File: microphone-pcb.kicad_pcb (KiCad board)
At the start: 4 copper layers, 10.7 x 11 mm, 9 parts, among them J1 JST_SUR_1x5_BM05B-SURS-TB-LF-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

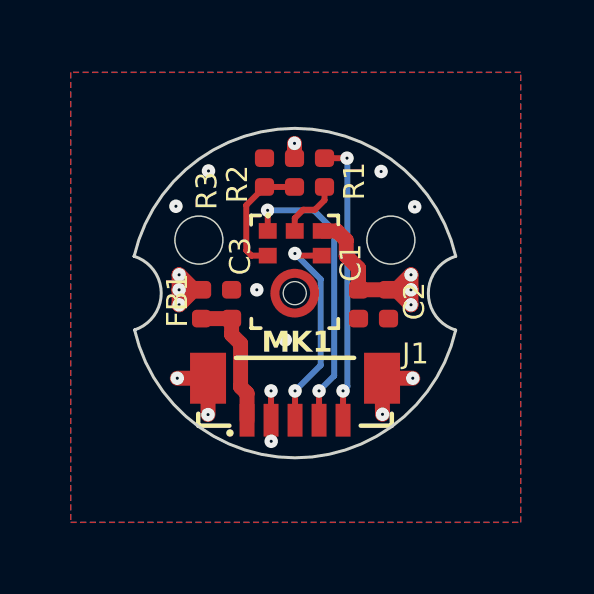
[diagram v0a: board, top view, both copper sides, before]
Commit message: [#71986]  Continue placement
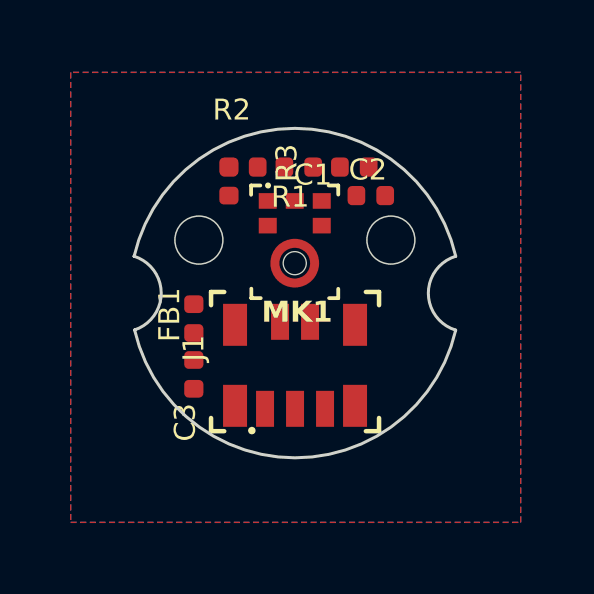
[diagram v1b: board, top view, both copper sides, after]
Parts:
- J1: value JST_SUR_1x5_BM05B-SURS-TB-LF-SN -> Conn_FFC_Molex_5019510550; footprint antmicro-footprints:Conn_JST_SUR_1x5_BM05B-SURS-TF-LF-SN -> antmicro-footprints:Conn_FFC_Molex_5019510550
- moved C1 4.57 mm to (242.0, 142.7), turned to 180 degrees
- moved C2 3.67 mm to (242.5, 143.7), turned to 0 degrees
- moved C3 2.66 mm to (236.6, 149.6), turned to 90 degrees
- moved R2 1.72 mm to (238.3, 142.7), turned to 0 degrees
- moved R3 1.22 mm to (237.8, 143.2), turned to 90 degrees
- moved J1 1.00 mm to (240.0, 149.2)
- moved MK1 1.00 mm to (240.0, 145.9)
- moved R1 0.88 mm to (240.1, 142.7), turned to 0 degrees
- moved FB1 0.55 mm to (236.6, 147.8)
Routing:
- net VDD: track 11.1 -> 0.00 mm, vias 7 -> 0
- net /WS: track 9.72 -> 0.00 mm, vias 2 -> 0
- net /DATA: track 9.55 -> 0.00 mm, vias 2 -> 0
- net /BCLK: track 7.19 -> 0.00 mm, vias 2 -> 0
- net GND: track 6.15 -> 0.00 mm, vias 12 -> 0
- net VCC: track 4.60 -> 0.00 mm
- net /SELECT: track 4.16 -> 0.00 mm
- net Net-(MK1-DATA): track 2.11 -> 0.00 mm

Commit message: [#71986] Bump rev to 1.2.0, route connections
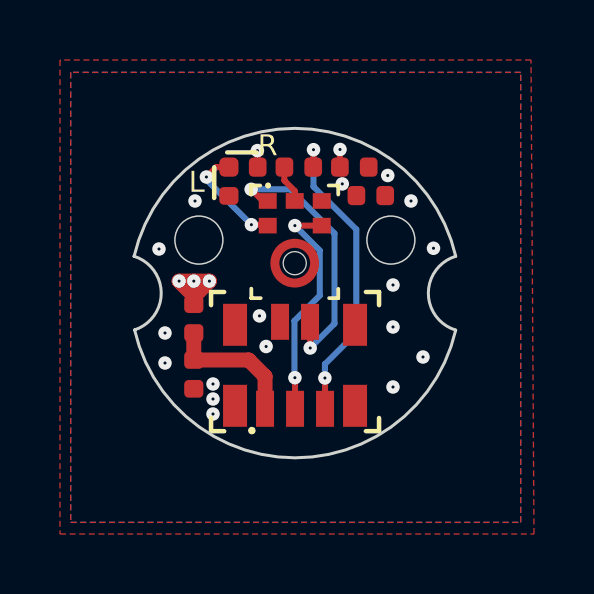
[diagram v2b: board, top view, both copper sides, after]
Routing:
- net /DATA: track 0.00 -> 10.2 mm, vias 0 -> 2
- net /WS: track 0.00 -> 9.13 mm, vias 0 -> 2
- net /BCLK: track 0.00 -> 7.75 mm, vias 0 -> 2
- net VDD: track 0.00 -> 4.88 mm, vias 0 -> 6
- net VCC: track 0.00 -> 4.58 mm
- net /SELECT: track 0.00 -> 3.66 mm, vias 0 -> 2
- net Net-(MK1-DATA): track 0.00 -> 1.41 mm
- net GND: vias 0 -> 16
- added copper zone on F.Cu, net VDD
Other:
- board text added: "Audio Microphone Rev. ${REVISION}"
- board text added: "L"
- board text added: "R"
- board text removed: "Audio Microphone"
